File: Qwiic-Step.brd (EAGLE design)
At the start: 38.1 x 38.1 mm, 56 parts, among them J1 PTH, J2 Qwiic Right Angle, J3 POWER_JACKSUPER_BOMB_DIGITY, J4 Qwiic Right Angle, J7 ISP, U1 A49885MM, U4 ATTINY84-ARDUINO

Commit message: temporary 4 layer
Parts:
- removed FID1, FID2: FIDUCIAL1X2, SparkFun-Aesthetics:FIDUCIAL-1X2
- removed J8: (no value), SparkFun-Connectors:1X01_NO_SILK
- removed JP3: (no value), SparkFun-Jumpers:SMT-JUMPER_2_NC_TRACE_SILK
- removed JP4: (no value), SparkFun-Jumpers:SMT-JUMPER_3_2-NC_TRACE_SILK
- removed JP5: (no value), BigEasyDriver_v11:SCREWTERMINAL-3.5MM-4_LOCK
- removed LED2: Yellow, SparkFun-LED:LED-1206
- removed LOGO2: SFE_LOGO_NAME_FLAME.1_INCH, SparkFun-Aesthetics:SFE_LOGO_NAME_FLAME_.1
- removed R13: 8.2k, SparkFun-Resistors:0603
- removed R16: 10k, SparkFun-Resistors:TRIMPOT-SMD-3MM-CLOSED
- removed R6, R7: 2.2k, SparkFun-Resistors:0603
- removed R8: 10k, SparkFun-Resistors:0603
- removed R9: 1k, SparkFun-Resistors:0603
- removed TP2: (no value), SparkFun-Connectors:PAD.03X.04
- removed U4: ATTINY84-ARDUINO, SparkFun-IC-Microcontroller:SO14
- added C14, C5: 0.1uF, SparkFun-Capacitors:0603
- added D4: RED, SparkFun-LED:LED-0603
- added D5: Yellow, SparkFun-LED:LED-0603
- added J5: ISP, SparkFun-Connectors:2X3
- added J9: (no value), SparkFun-Connectors:SCREWTERMINAL-3.5MM-2
- added JP13: JUMPER-SMT_2_NC_TRACE_SILK, SparkFun-Jumpers:SMT-JUMPER_2_NC_TRACE_SILK
- added R12: 4.7k, SparkFun-Resistors:0603
- added R14: 10k, SparkFun-Resistors:0603
- added R15: 1k, SparkFun-Resistors:0603
- added S1: Tall Switch, SparkFun-Switches:TACTILE_SWITCH_SMD_5.2MM
- added U$1: (no value), buzzard_labels (8):3V30
- added U$10, U$11: (no value), buzzard_labels (14):GND1
- added U$12: (no value), buzzard_labels (14):RXI3
- added U$13: (no value), buzzard_labels (14):TXO4
- added U$14: (no value), buzzard_labels (14):VIN2
- added U$15: (no value), buzzard_labels (15):A#0
- added U$16: (no value), buzzard_labels (15):A#1
- added U$17: (no value), buzzard_labels (15):B#2
- added U$18: (no value), buzzard_labels (15):B#3
- added U$19: (no value), SparkX:SPARKX-MEDIUM
- added U$2: (no value), buzzard_labels (8):3V37
- added U$3: (no value), buzzard_labels (8):GND8
- added U$4: (no value), buzzard_labels (13):STAT5
- added U$5: (no value), buzzard_labels (8):SCL5
- added U$6: (no value), buzzard_labels (8):SDA6
- added U$7: (no value), buzzard_labels (8):STEP4
- added U$8: (no value), buzzard_labels (8):VIN3
- added U$9: (no value), buzzard_labels (14):DTR5
- added U2: ATMEGA328P_TQFP, SparkFun-IC-Microcontroller:TQFP32-08
- added Y1: 16MHz, SparkFun-Clocks:RESONATOR-SMD-3.2X1.3
- C2: value 0.1uF -> 10nF
- C4: value 10uF -> 0.1uF
- D2: value RED -> GREEN
- J6: device SparkFun-Connectors:1X01_NO_SILK -> SparkFun-Connectors:SCREWTERMINAL-3.5MM-4
- J7: value ISP -> (none); device SparkFun-Connectors:2X3_TEST_POINTS -> SparkFun-Connectors:1X06_NO_SILK
- JP1, JP11: value (none) -> JUMPER-SMT_2_NC_TRACE_SILK
- JP2: value (none) -> INT; device SparkFun-Jumpers:SMT-JUMPER_2_NO_SILK -> SparkFun-Jumpers:SMT-JUMPER_2_NC_TRACE_SILK
- R3: value 100k -> 33k
- moved LOGO1 93.5 mm to (38.1, 41.9)
- moved C4 86.6 mm to (18.8, 37.0)
- moved D3 83.9 mm to (17.1, 23.4), turned to 180 degrees
- moved JP11 79.8 mm to (17.1, 22.1), flipped to the bottom, turned to 180 degrees
- moved R11 76.8 mm to (17.1, 22.1), turned to 180 degrees
- moved R3 70.9 mm to (25.9, 12.4)
- moved J6 41.3 mm to (40.8, 17.0), turned to 90 degrees
- moved JP1 37.1 mm to (38.1, 7.62), turned to 180 degrees
- moved R1 37.1 mm to (38.1, 7.62)
- moved J7 34.4 mm to (17.9, 43.2), flipped to the top, turned to 180 degrees
- moved C1 26.9 mm to (10.5, 34.9)
- moved C2 23.0 mm to (29.0, 12.4)
- moved D2 20.5 mm to (2.79, 13.0)
- moved J1 16.5 mm to (38.1, 1.27)
- moved C7 16.1 mm to (24.0, 17.8), turned to 270 degrees
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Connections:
- removed net !INT!: R2.1, U4.13
- removed net !RST: J7.5, R8.1, U4.4
- removed net N$2: D2.A, R9.1
- removed net N$3: R13.2, R16.1
- removed net N$5 (its old number): JP3.1, R9.2
- removed net SCL_PU1: JP4.1, R6.2
- removed net SDA_PU1: JP4.3, R7.2
- new net !RST!: C4.2, J5.5, R14.1, S1.3, S1.4, U2.29
- new net AREF: C5.1, U2.20
- new net DTR: C4.1, J7.1
- new net INT: R2.1, U2.32
- new net N$12: D2.A, R12.2
- new net N$13: U2.7, Y1.1
- new net N$14: U2.8, Y1.3
- new net N$26: D4.A, R15.1
- new net N$27: JP13.1, R15.2
- new net RXI: J7.3, U2.30
- new net SCK: R12.1, U2.17
- new net TXO: J7.2, U2.31
- net !ENABLE!: now also U2.15; no longer U4.11
- net !RESET!: now also U2.12
- net !SLEEP!: now also U2.2
- net 3.3V: now also C14.1, J5.2, JP13.2, R14.2, U2.18, U2.4, U2.6; no longer C2.1, J7.2, JP3.2, JP4.2, R13.1, R8.2, U4.1
- net ADR: now also U2.13; no longer U4.12
- net COILA+: now also J6.1; no longer JP5.4
- net COILA-: now also J6.2; no longer JP5.3
- net COILB+: now also J6.4; no longer JP5.1
- net COILB-: now also J6.3; no longer JP5.2
- net CUR_REF: now also C2.1; no longer C4.2, R16.2, TP2.P$1
- net CUR_REF_PWM: now also U2.1; no longer U4.5
- net DIR: now also U2.14; no longer U4.10
- net GND: now also C14.2, C5.2, D4.C, D5.C, J5.6, J7.5, J9.1, S1.1, S1.2, U2.21, U2.3, U2.5, Y1.2; no longer C4.1, J8.1, LED2.C, R16.3, U4.14
- net MS1: now also J5.1, U2.11; no longer J7.1, U4.8
- net MS2: now also U2.10; no longer U4.3
- net MS3: now also U2.9; no longer U4.2
- net N$10: now also D5.A; no longer LED2.A
- net N$7: now also J9.2; no longer J6.1
- net SCL: now also J5.3, U2.28; no longer J7.3, R6.1, U4.9
- net SDA: now also J5.4, U2.27; no longer J7.4, R7.1, U4.7
- net STEP: now also U2.22; no longer U4.6
- net VIN: now also J7.4
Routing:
- net SDA: track 0.00 -> 79.4 mm, vias 0 -> 4
- net !RST!: track 0.00 -> 75.9 mm, vias 0 -> 3
- net SCL: track 0.00 -> 73.5 mm, vias 0 -> 5
- net VIN: track 0.00 -> 53.0 mm, vias 0 -> 4
- net 3.3V: track 0.00 -> 46.9 mm, vias 0 -> 8
- net STEP: track 0.00 -> 39.4 mm, vias 0 -> 6
- net MS1: track 0.00 -> 36.4 mm
- net TXO: track 0.00 -> 36.0 mm, vias 0 -> 1
- net !ENABLE!: track 10.2 -> 35.2 mm, vias 0 -> 2
- net DIR: track 0.00 -> 24.0 mm, vias 0 -> 2
- net !RESET!: track 0.00 -> 21.9 mm, vias 0 -> 2
- net !SLEEP!: track 0.00 -> 20.3 mm
- net MS2: track 0.00 -> 16.6 mm
- net MS3: track 0.00 -> 15.5 mm
- net CUR_REF_PWM: track 0.00 -> 13.2 mm
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- added copper zone on layer 2, net 3.3V
- removed copper zone on layer 16, net GND
- removed copper zone on layer 2, net VCC
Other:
- board size 38.1 x 38.1 mm -> 44.5 x 44.5 mm
- board text removed: "+"
- board text removed: "7-35V DC"
- board text removed: "A"
- board text removed: "ADJ"
- board text removed: "B"
- board text removed: "CUR"
- board text removed: "GND"
- board text removed: "MOTOR"
- board text removed: "Motor Coils"
- board text removed: "PWR"
- board text removed: "PWR IN"

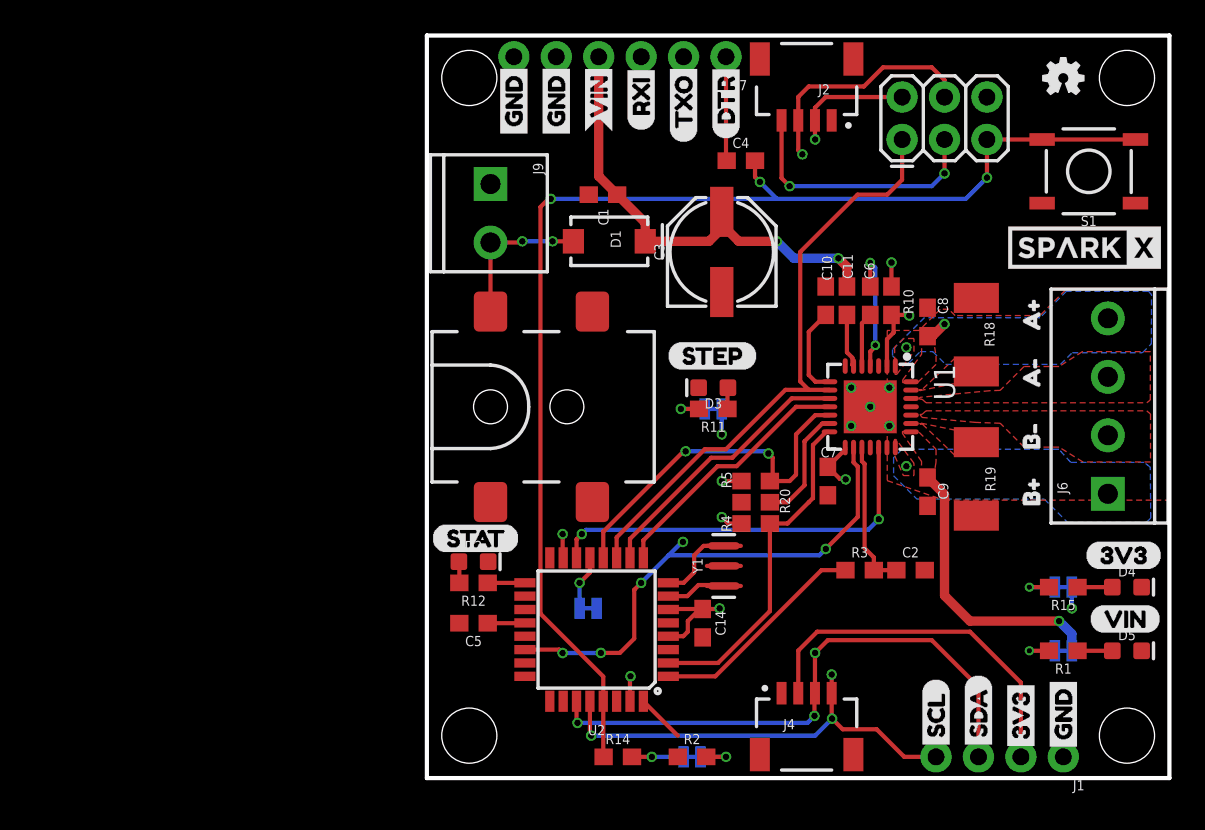
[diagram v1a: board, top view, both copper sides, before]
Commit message: Reduce to 2 layers
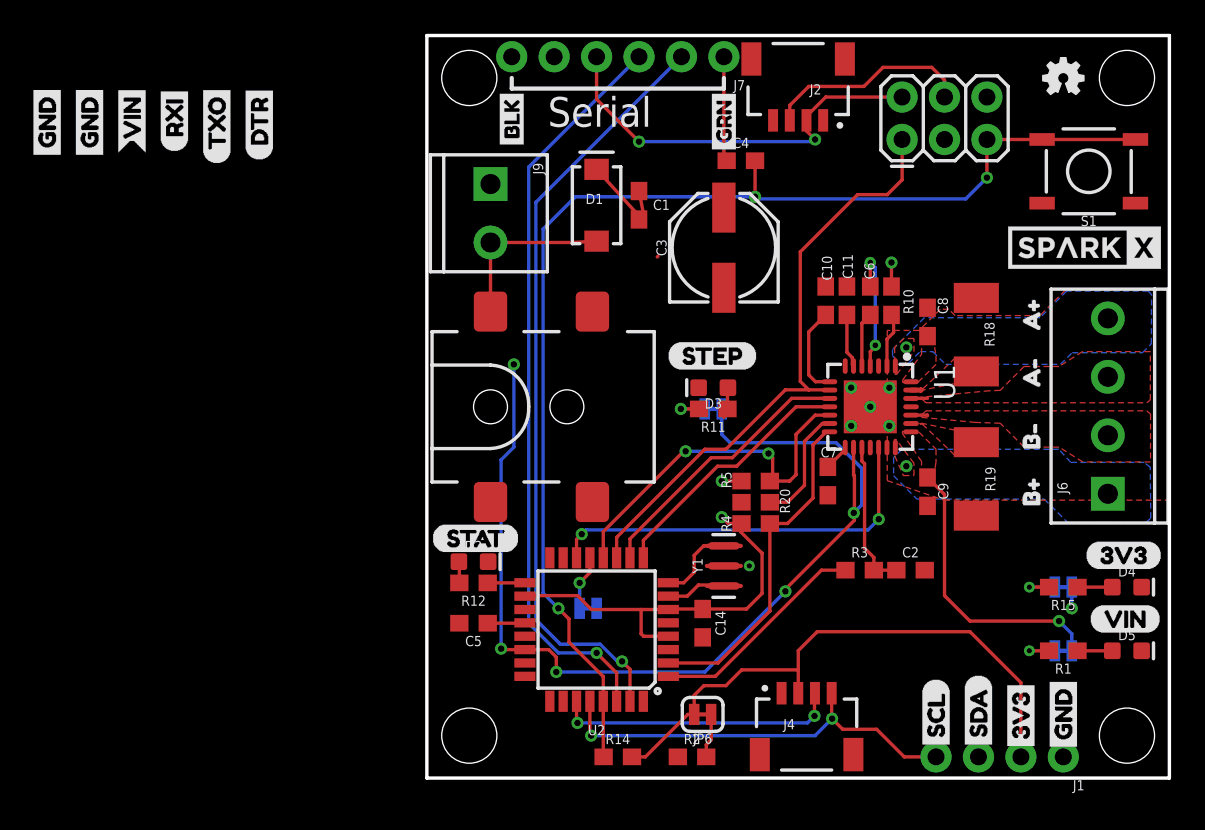
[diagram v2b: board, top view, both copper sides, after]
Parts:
- added U$20, U$21: (no value), buzzard_labels:BLK2
- added U$22, U$28: (no value), buzzard_labels:GRN1
- moved U$10 28.0 mm to (-20.2, 36.8)
- moved U$11 28.0 mm to (-22.7, 36.8)
- moved U$13 28.0 mm to (-12.6, 36.7)
- moved U$12 28.0 mm to (-15.1, 37.5)
- moved U$14 28.0 mm to (-17.7, 37.3)
- moved U$9 28.0 mm to (-10.0, 37.0)
- moved JP6 2.62 mm to (16.5, 3.81), flipped to the top, turned to 180 degrees
- moved D1 2.29 mm to (10.2, 34.3), turned to 90 degrees
- moved C1 2.25 mm to (12.7, 34.3), turned to 270 degrees
- moved J2 0.51 mm to (22.2, 39.4)
- moved C3 0.28 mm to (17.8, 31.8)
- moved J7 0.13 mm to (17.8, 43.2)
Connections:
- net 3.3V: now also J7.4
- net VIN: no longer J7.4
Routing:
- net SDA: track 79.4 -> 29.5 mm, vias 4 -> 2
- net SCL: track 73.5 -> 25.7 mm, vias 5 -> 2
- net RXI: track 0.00 -> 44.8 mm, vias 0 -> 1
- net 3.3V: track 46.9 -> 89.2 mm, vias 8 -> 6
- net !ENABLE!: track 35.2 -> 3.28 mm, vias 2 -> 0
- net VIN: track 53.0 -> 22.8 mm, vias 4 -> 1
- net STEP: track 39.4 -> 61.4 mm, vias 6 -> 5
- net TXO: track 36.0 -> 46.1 mm
- net INT: track 2.92 -> 0.00 mm
- net !RST!: track 75.9 -> 74.4 mm
- net N$7: track 9.13 -> 10.5 mm, vias 2 -> 0
- net COILA-: track 0.00 -> 0.99 mm
- net COILB-: track 0.00 -> 0.99 mm
- net N$31: track 0.00 -> 0.61 mm
- net N$1: track 1.28 -> 1.88 mm
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- added copper zone on layer 16, net GND
- added copper zone on layer 1, net VIN
- removed copper zone on layer 2, net 3.3V
- removed copper zone on layer 15, net GND
- removed copper zone on layer 1, net V+
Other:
- board text added: "Serial"
- board text removed: "VCC"
